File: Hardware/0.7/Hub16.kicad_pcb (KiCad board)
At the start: 2 copper layers, 89 x 100 mm, 132 parts, among them J1 USB_C_Receptacle_USB2.0, J2 AVR-ISP-6, J3 USB_C_Receptacle_USB2.0, J4 USB_C_Receptacle_USB2.0, J5 USB_C_Receptacle_USB2.0, K1 KEYSW, K11 KEYSW, K12 KEYSW, K13 KEYSW, K14 KEYSW, K16 KEYSW, K17 KEYSW, K18 KEYSW, K19 KEYSW, K2 KEYSW, K3 KEYSW, K4 KEYSW, K6 KEYSW, K7 KEYSW, K8 KEYSW, K9 KEYSW, SW1 KMR2, SW2 Rotary_Encoder_Switch, SW3 Rotary_Encoder_Switch, U1 USBLC6-2SC6, U2 ATMEGA32U4, U3 CY7C65632-28LTXCT, U4 USBLC6-2SC6, U5 USBLC6-2SC6, U6 USBLC6-2SC6, Y1 16MHz, Y2 12MHz

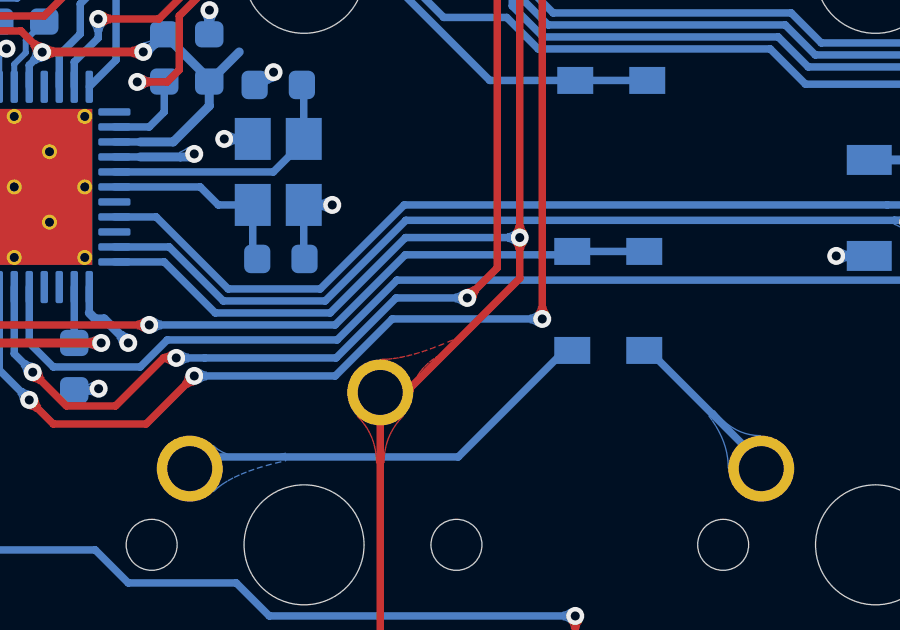
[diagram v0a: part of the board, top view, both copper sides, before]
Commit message: fix v0.5 bom + release prototypes
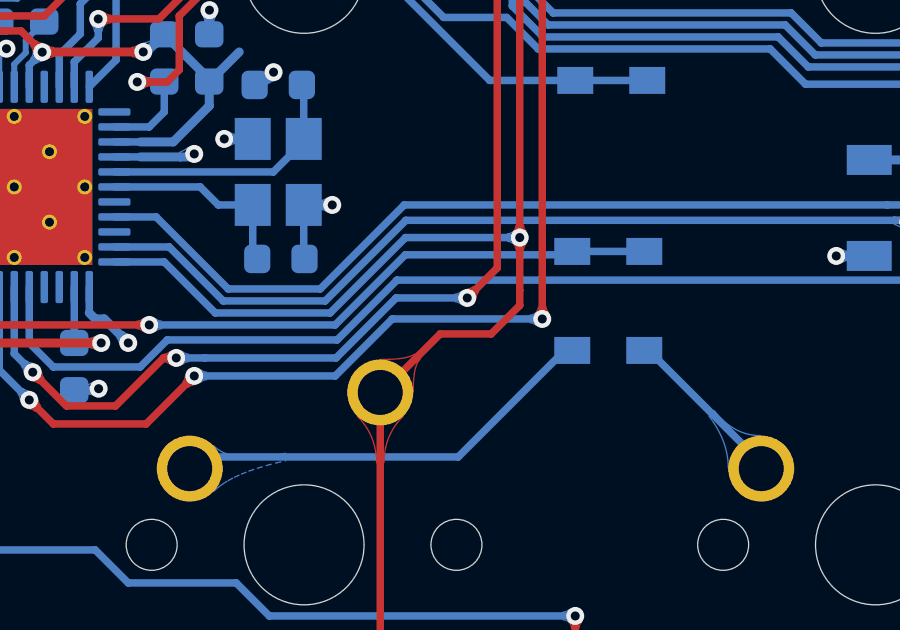
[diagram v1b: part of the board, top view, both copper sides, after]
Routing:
- net /col3: track 78.4 -> 79.9 mm
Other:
- board text added: "JLCJLCJLC"

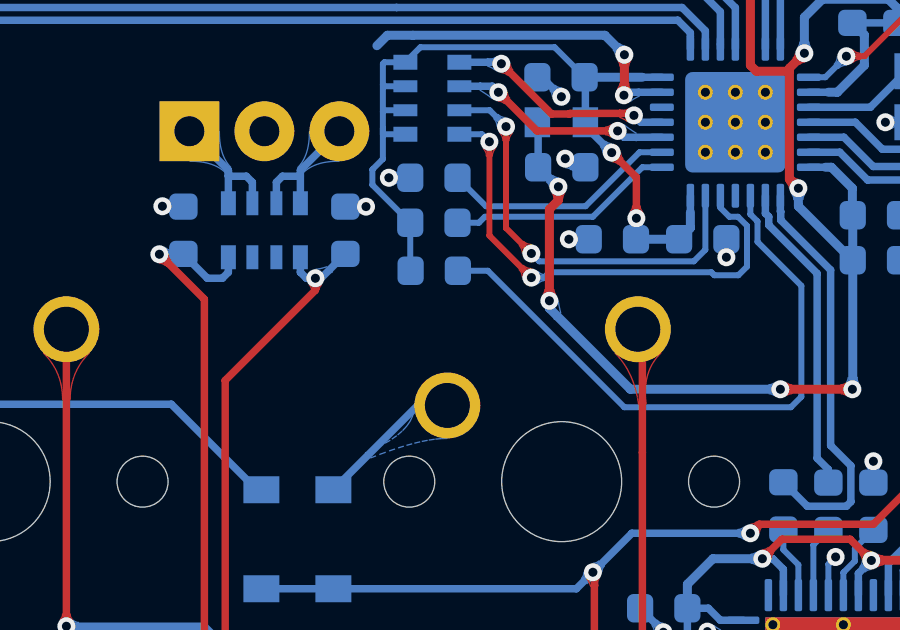
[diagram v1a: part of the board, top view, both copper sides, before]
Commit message: move res with HS interference
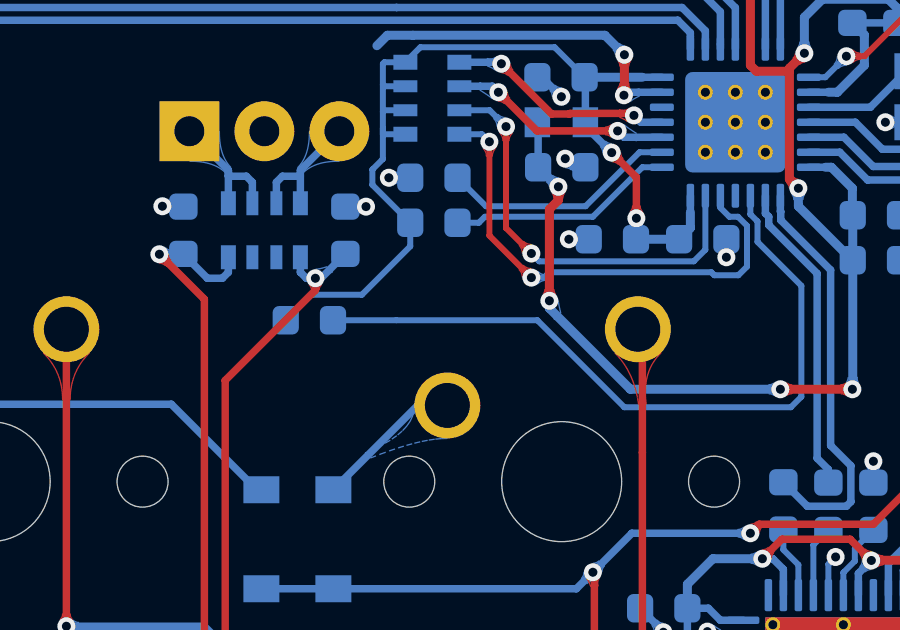
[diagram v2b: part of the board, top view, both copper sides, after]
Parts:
- moved R10 4.48 mm to (74.0, 63.8)
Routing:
- net +3V3: track 29.7 -> 34.0 mm
- net Net-(R10-Pad1): track 20.9 -> 24.4 mm
